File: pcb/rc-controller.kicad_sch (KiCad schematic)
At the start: 3 parts, among them M1 Motor_DC, M2 Motor_DC, U1 STM32F401RCTx

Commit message: Update .gitignore
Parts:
- added C1, C11, C2: 100n, Capacitor_SMD:C_0402_1005Metric, symbol Device:C
- added C10: 2.2u, Capacitor_SMD:C_0603_1608Metric, symbol Device:C
- added C12, C14: 10u, symbol Device:C
- added C13, C15, C3, C4, C5, C6, C7, C8: 100n, symbol Device:C
- added C9: 1u, Capacitor_SMD:C_0402_1005Metric, symbol Device:C
- added D1: LEDB, LED_SMD:LED_0603_1608Metric, symbol Device:LED
- added D2: LEDR, symbol Device:LED
- added D3: LEDG, symbol Device:LED
- added J1: USB_C_Receptacle_USB2.0, Connector_USB:USB_C_Receptacle_GCT_USB4105-xx-A_16P_TopMnt_Horizontal, symbol Connector:USB_C_Receptacle_USB2.0
- added PB1, PB2, PB3, PB4, PB5: SW_Push, symbol Switch:SW_Push
- added R1: 10k, symbol Device:R
- added R10, R2, R9: 1k, Resistor_SMD:R_0402_1005Metric, symbol Device:R
- added R3, R6: 10k, Resistor_SMD:R_0402_1005Metric, symbol Device:R
- added R4, R5: 5k1, Resistor_SMD:R_0402_1005Metric, symbol Device:R
- added R7: 100k, symbol Device:R
- added R8: 1k, symbol Device:R
- added RE1, RE2: RotaryEncoder_Switch, symbol Device:RotaryEncoder_Switch
- added SW1, SW2: SW_SPDT, symbol Switch:SW_SPDT
- added U2: LPS22HB, Package_LGA:ST_HLGA-10_2x2mm_P0.5mm_LayoutBorder3x2y, symbol Sensor_Pressure:LPS22HB
- added U3: SRV05-4, Package_TO_SOT_SMD:SOT-23-6, symbol Power_Protection:SRV05-4
- added U4: NE555D, Package_SO:SOIC-8_3.9x4.9mm_P1.27mm, symbol Timer:NE555D
- added U5: ICM-42670-P, Package_LGA:LGA-14_3x2.5mm_P0.5mm_LayoutBorder3x4y, symbol MySymbols:ICM-42670-P
- added U6: TP4057-42, Package_TO_SOT_SMD:TSOT-23-6, symbol User_Symbols:TP4057-42
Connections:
- net +3V3: now reaches U1.1 (VBAT)
- net +3V3: now also U1.19 (VDD), U1.32 (VDD), U1.48 (VDD), U1.64 (VDD), C1.1, C10.1, C11.1, C2.1, C4.1, C5.1, C6.1, C7.1, C8.1, U2.1 (Vdd_IO), U2.10 (VDD), U5.5 (VDDIO), U5.8 (VDD)
- net GND: now reaches U1.12 (VSSA)
- net GND: now also U1.18 (VSS), U1.31 (VSS), U1.47 (VSS), U1.63 (VSS), C1.2, C10.2, C11.2, C12.2, C13.2, C14.2, C15.2, C2.2, C3.2, C4.2, C5.2, C6.2, C7.2, C8.2, C9.2, D1.1 (K), J1.A1 (GND), J1.A12 (GND), J1.B1 (GND), J1.B12 (GND), J1.S1 (SHIELD), R1.2, R4.2, R5.2, R6.2, U2.3 (RES), U2.8 (GND), U2.9 (GND), U3.2 (VN), U4.1 (GND), U5.10 (RESV), U5.11 (RESV), U5.2 (RESV), U5.3 (RESV), U5.6 (GND), U5.7 (FSYNC), U6.2 (GND)
- net BOOT0: now reaches U1.60 (BOOT0)
- net BOOT0: now also R1.1
- net nRST: now reaches U1.7 (NRST)
- net nRST: now also C3.1
- new net: D2.1 (K), U6.1 (CHRG)
- new net: D2.2 (A), R9.2
- new net: D3.2 (A), R10.2
- new net: J1.A5 (CC1), R5.1
- new net: D3.1 (K), U6.5 (STDBY)
- new net: J1.B5 (CC2), R4.1
- new net DRDY: U2.7 (INT_DRDY)
- new net GCS: U5.12 (CS)
- new net GINT1: U5.4 (INT1)
- new net GINT2: U5.9 (INT2)
- new net GSCLK: U5.13 (SCL/SCLK)
- new net GSDI: U5.14 (SDA/SDIO/SDI)
- new net GSDO: U5.1 (SDO/AD0)
- new net OUT: R9.1, U4.3 (Q)
- new net SCK: U2.2 (SCL)
- new net SDI: U2.4 (SDA)
- new net SDO: U2.5 (SA0)
- new net SNSBUS: R3.2, R6.1
- new net THRESH: R7.1, R8.2, U4.7 (DIS)
- new net TREF: C13.1, U4.5 (CV)
- new net TRIG: C14.1, R7.2, U4.2 (TR), U4.6 (THR)
- new net USB_D+: J1.A6 (D+), J1.B6 (D+), U3.3 (IO2)
- new net USB_D-: J1.A7 (D-), J1.B7 (D-), U3.1 (IO1)
- new net VBATT: C12.1, U6.3 (BAT)
- new net VBLED: D1.2 (A), R2.2
- new net VBUS: C15.1, C9.1, J1.A4 (VBUS), J1.A9 (VBUS), J1.B4 (VBUS), J1.B9 (VBUS), R10.1, R2.1, R3.1, R8.1, U3.5 (VP), U4.4 (R), U4.8 (VCC), U6.4 (VCC)
- new net nCS: U2.6 (~{CS})
- no-connect marks 0 -> 4
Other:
- note added: "Battery Managment"
- note added: "ESD Protection"
- note added: "Gyroscope + Accelerometer"
- note added: "JOYSTICK"
- note added: "OLED"
- note added: "USB Full Speed"
- note added: "nrf24L01P"
- note removed: "C2834912"
- note removed: "C2834937"
- note removed: "C496169"
- note removed: "C499339"
- note removed: "C5248081"
- note removed: "C5446826"
- moved on the sheet: U1

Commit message: Finish schematic
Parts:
- removed D2: LEDR, symbol Device:LED
- removed D3: LEDG, symbol Device:LED
- removed M2: Motor_DC, symbol Motor:Motor_DC
- removed PB2, PB3, PB4, PB5: SW_Push, symbol Switch:SW_Push
- removed U4: NE555D, Package_SO:SOIC-8_3.9x4.9mm_P1.27mm, symbol Timer:NE555D
- added BT1: Battery_Cell, symbol Device:Battery_Cell
- added C16, C18: 10u, symbol Device:C
- added C17: 1u, symbol Device:C
- added C19, C20, C21: 100u, symbol Device:C
- added D2, D4: SS24, Diode_SMD:D_SMA, symbol Diode:SS24
- added FB1: FerriteBead, symbol Device:FerriteBead
- added JY1, JY2: COM-09032, symbol User_Symbols:COM-09032
- added L1: 10u, symbol Device:L
- added Q1, Q2: AO3401A, Package_TO_SOT_SMD:SOT-23, symbol Transistor_FET:AO3401A
- added Q3, Q4: AO3400A, Package_TO_SOT_SMD:SOT-23, symbol Transistor_FET:AO3400A
- added R11, R16, R17: 200k, symbol Device:R
- added R12: 340k, symbol Device:R
- added R13, R14: 47k, symbol Device:R
- added R15: 2k, symbol Device:R
- added SW3, SW4, SW5, SW6: SW_DPST, symbol Switch:SW_DPST
- added U4: TX4401, Package_SO:SOP-8-1EP_4.57x4.57mm_P1.27mm_EP4.57x4.45mm, symbol User_Symbols:TX4401
- added U7: nrf24L01P_PA_LNA, symbol User_Symbols:nrf24L01P_PA_LNA_Module
- added U8: SSD1306, symbol User_Symbols:SSD1306_128x32
- C1: footprint Capacitor_SMD:C_0402_1005Metric -> (none)
- C14: value 10u -> 1n5
- C15: value 100n -> 22u
- R10: value 1k -> 15k; footprint Resistor_SMD:R_0402_1005Metric -> (none)
- R7: value 100k -> 56k
- R8: value 1k -> 4k7
- R9: value 1k -> 1m; footprint Resistor_SMD:R_0402_1005Metric -> (none)
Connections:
- net SCK is gone; now on net SNSCK: U2.2 (SCL)
- net SDI is gone; now on net SNMOSI: U2.4 (SDA)
- net SDO is gone; now on net SNMISO: U2.5 (SA0)
- net TREF is gone; now on an unnamed net: C13.1
- net +3V3: now also C15.1, SW1.1 (A), SW2.1 (A), C18.1, C19.1, C21.1, FB1.1, JY1.A1 (XH), JY1.A2 (YH), JY2.A1 (XH), JY2.A2 (YH), Q1.2 (S), R12.1, U4.5 (VOUT), U7.2 (VCC)
- net GND: now also M1.2 (-), PB1.1, R7.2, RE1.C, RE1.S2, RE2.C, RE2.S2, SW1.3 (C), SW2.3 (C), BT1.2 (-), C16.2, C17.2, C18.2, C19.2, C20.2, C21.2, JY1.B1 (XL), JY1.B2 (YL), JY1.MP (Shield), JY1.S2 (SWB), JY2.B1 (XL), JY2.B2 (YL), JY2.MP (Shield), JY2.S2 (SWB), Q3.2 (S), Q4.2 (S), R11.2, R14.2, R15.2, R16.2, SW3.2, SW3.4, SW4.2, SW4.4, SW5.2, SW5.4, SW6.2, SW6.4, U4.9 (GND), U7.1 (GND), U8.4 (GND); no longer C14.2
- net SNSBUS: now also Q3.1 (G)
- net VBATT: now also BT1.1 (+), C16.1, Q2.2 (S), R13.1; no longer C12.1
- net VBUS: now also D4.2 (A); no longer C15.1, R10.1, R8.1, U6.4 (VCC)
- net TSW2: now reaches SW2.2 (B)
- net CHRG: now reaches U6.1 (CHRG)
- net at R9.2: now also U4.7 (EN)
- net at M1.1 (+): now also D2.1 (K)
- net TSW1: now reaches SW1.2 (B)
- net RE2A: now reaches RE2.A
- net RE2B: now reaches RE2.B
- net RE2SW: now reaches RE2.S1
- net at R10.2: now also R11.1, R12.2, U4.8 (FB)
- net at PB1.2: now also Q2.1 (G), Q3.3 (D), Q4.3 (D), R13.2
- net STDBY: now reaches U6.5 (STDBY)
- net at U6.6 (PROG): now also R15.1
- net RE1A: now reaches RE1.A
- net RE1B: now reaches RE1.B
- net RE1SW: now reaches RE1.S1
- net GSCLK renamed SNSCK
- net GSDI renamed SNMOSI
- net GSDO renamed SNMISO
- net OUT renamed VPWR
- net VPWR: now also C12.1, Q2.3 (D), R17.1, U4.6 (VIN)
- net THRESH: no longer names the net of R7.1, R8.2
- net TRIG: no longer names the net of C14.1
- net TRIG: now also R10.1; no longer R7.2
- net nCS renamed PCS
- new net: D2.2 (A), Q1.3 (D)
- new net: C14.2, U4.1 (VC)
- new net: C17.1, D4.1 (K), U6.4 (VCC)
- new net: L1.1, U4.3 (SW1)
- new net: L1.2, U4.4 (SW2)
- new net: R8.1, U4.2 (RT)
- new net BREF: R16.1, R17.2
- new net BT1: SW3.1, SW3.3
- new net BT2: SW4.1, SW4.3
- new net BT3: SW5.1, SW5.3
- new net BT4: SW6.1, SW6.3
- new net JY1SW: JY1.S1 (SWA)
- new net JY1X: JY1.C1 (X)
- new net JY1Y: JY1.C2 (Y)
- new net JY2SW: JY2.S1 (SWA)
- new net JY2X: JY2.C1 (X)
- new net JY2Y: JY2.C2 (Y)
- new net MTR: Q1.1 (G)
- new net OPWR: C20.1, FB1.2, U8.3 (VCC)
- new net PWRON: Q4.1 (G), R14.1
- new net RFCE: U7.3 (CE)
- new net RFCS: U7.4 (~{CSN})
- new net RFIRQ: U7.8 (IRQ)
- new net RFMISO: U7.7 (MISO)
- new net RFMOSI: U7.6 (MOSI)
- new net RFSCK: U7.5 (SCK)
- new net SCL: U8.2 (SCL)
- new net SDA: U8.1 (SDA)
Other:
- note added: "Joysticks"
- note added: "Pressure Sensor"
- note added: "Rotary Encoders"
- note added: "Switches"
- note added: "Vibration"
- note removed: "JOYSTICK"
- moved on the sheet: C10, C11, C2, C3, C4, C5, C6, C7, C8, C9, D1, J1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

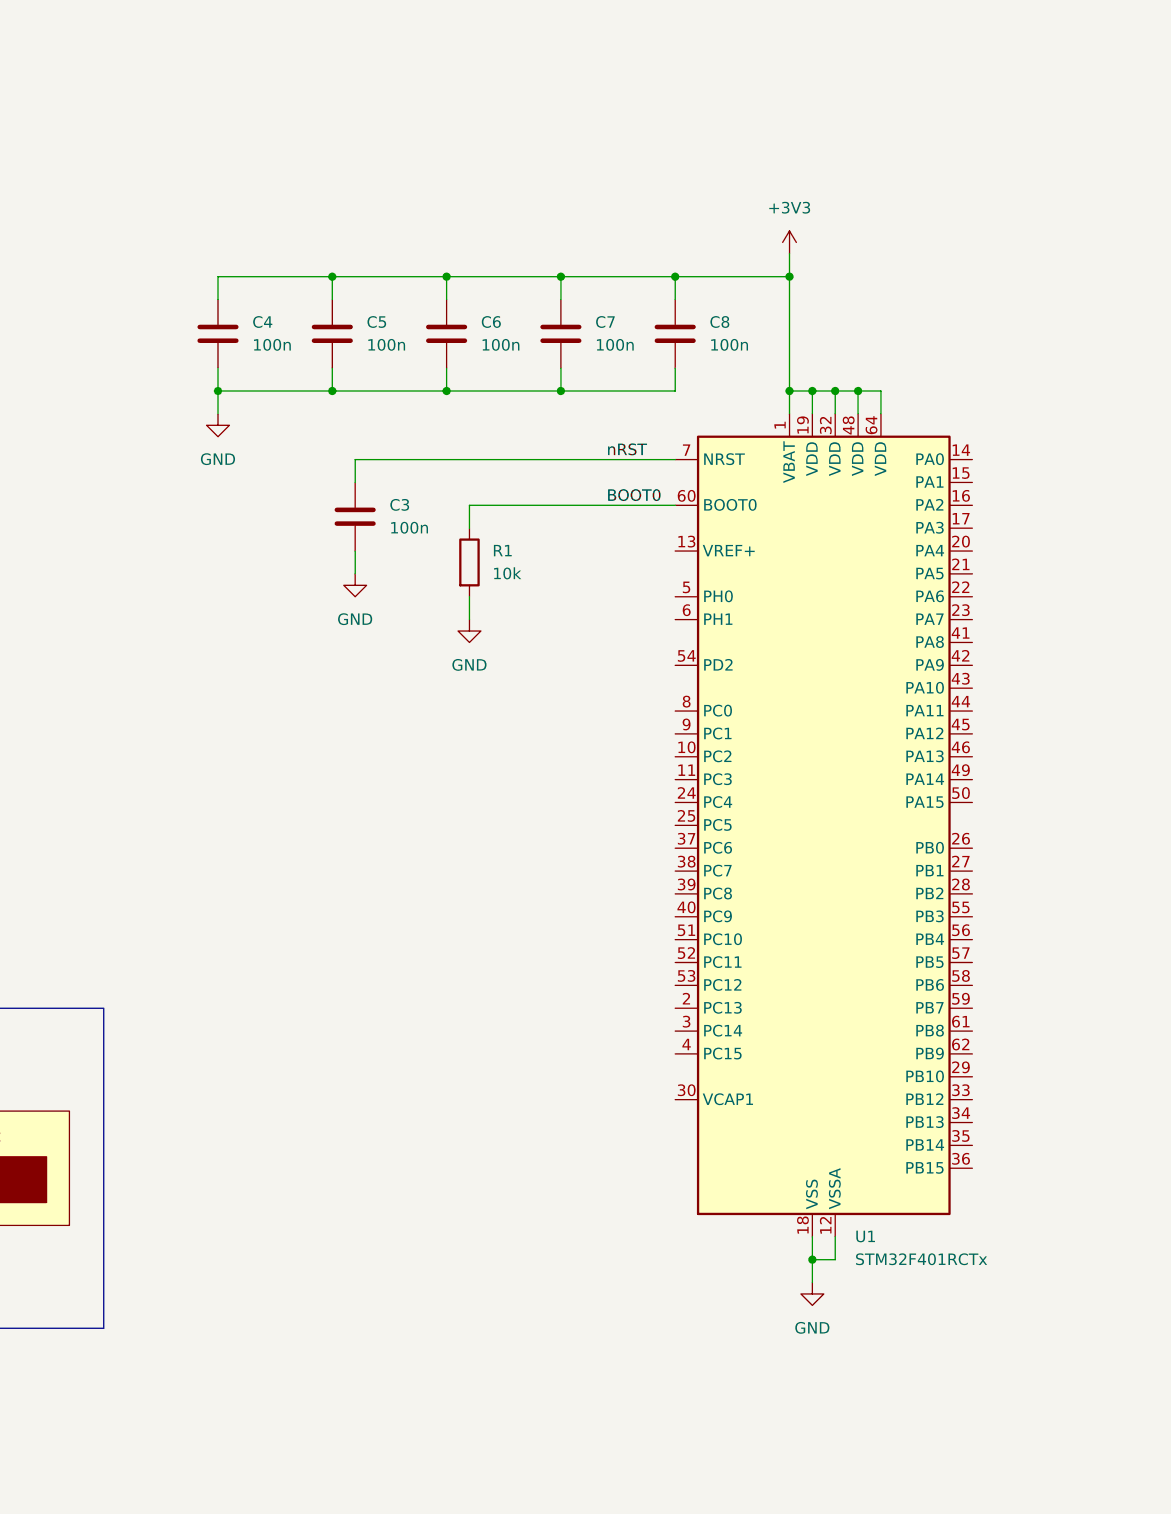
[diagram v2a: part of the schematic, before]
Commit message: Create STM32 project
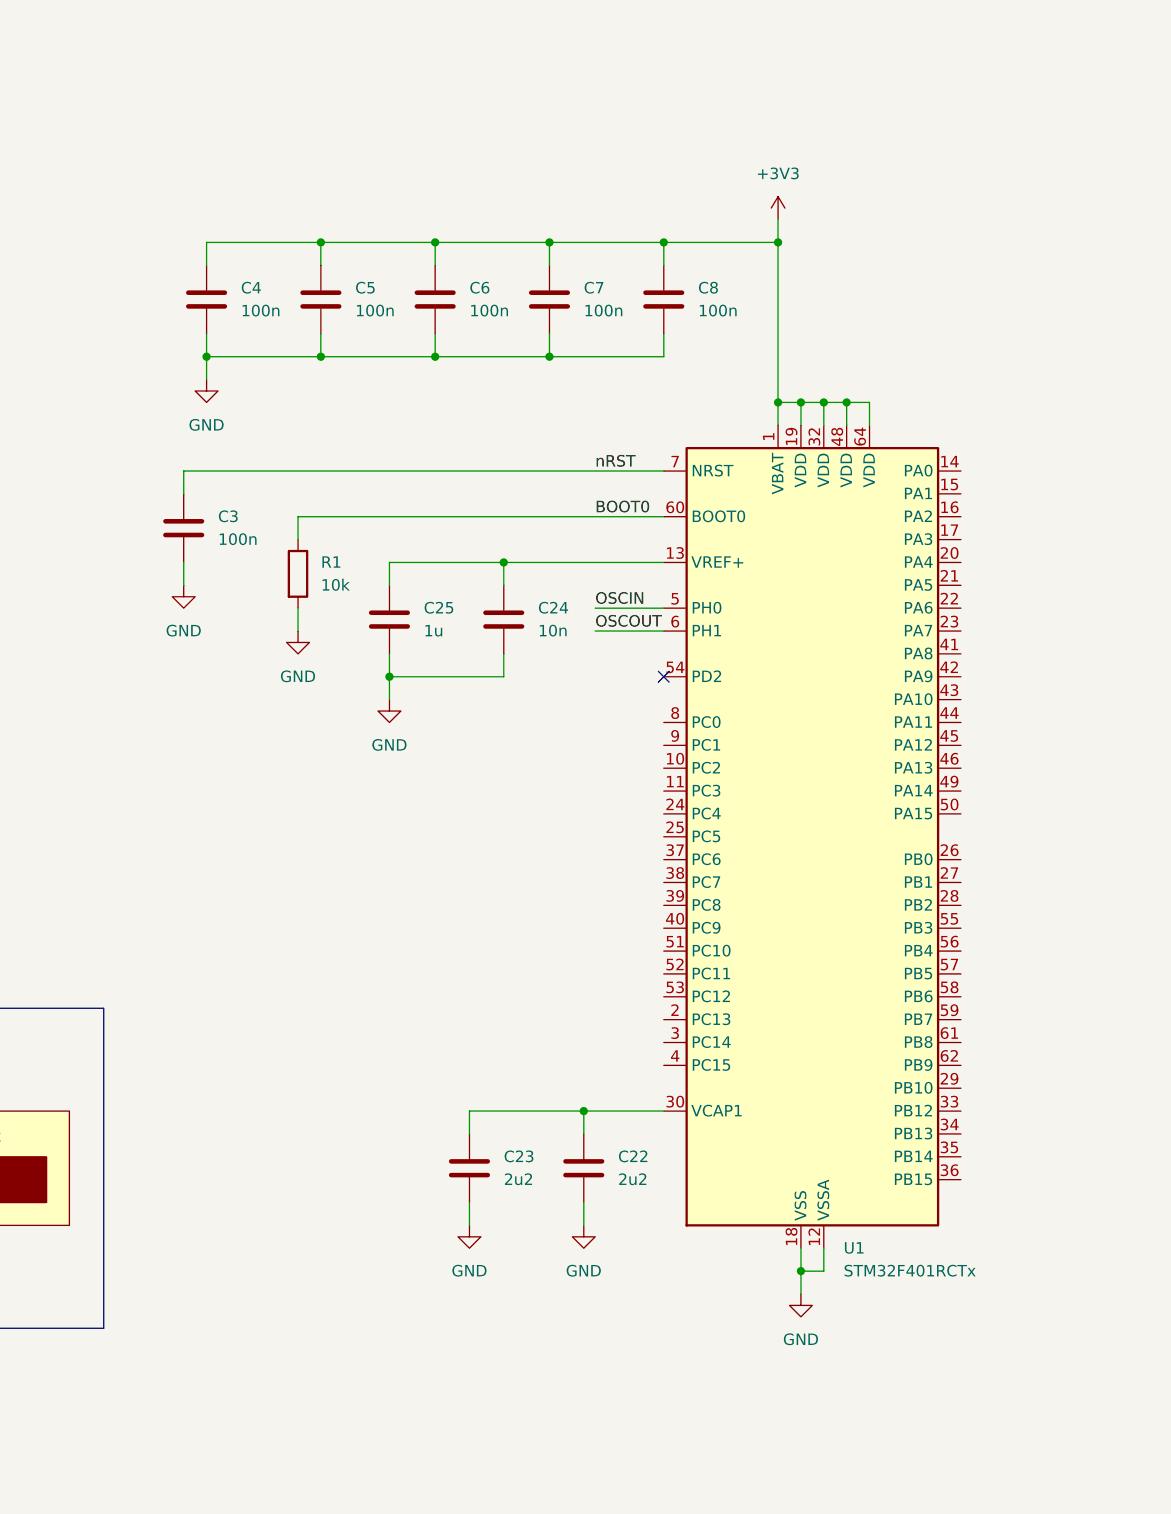
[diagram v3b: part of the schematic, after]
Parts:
- added C22, C23: 2u2, symbol Device:C
- added C24: 10n, symbol Device:C
- added C25: 1u, symbol Device:C
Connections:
- net GND: now also C22.2, C23.2, C24.2, C25.2
- net at U1.13 (VREF+): now also C24.1, C25.1
- net at U1.30 (VCAP1): now also C22.1, C23.1
- net OSCIN: now reaches U1.5 (PH0)
- net OSCOUT: now reaches U1.6 (PH1)
- no-connect marks 4 -> 5
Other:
- moved on the sheet: C3, C4, C5, C6, C7, C8, R1, U1
